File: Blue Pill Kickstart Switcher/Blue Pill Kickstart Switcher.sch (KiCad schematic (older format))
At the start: 23 parts, among them J1 Conn_01x02, J2 Conn_01x03, J3 Conn_01x03, J4 Conn_01x04, J5 Conn_01x03, J6 Conn_01x02, J7 Conn_01x02, J8 Conn_01x02, J9 Conn_01x02, U1 Conn_02x21_Counter_Clockwise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

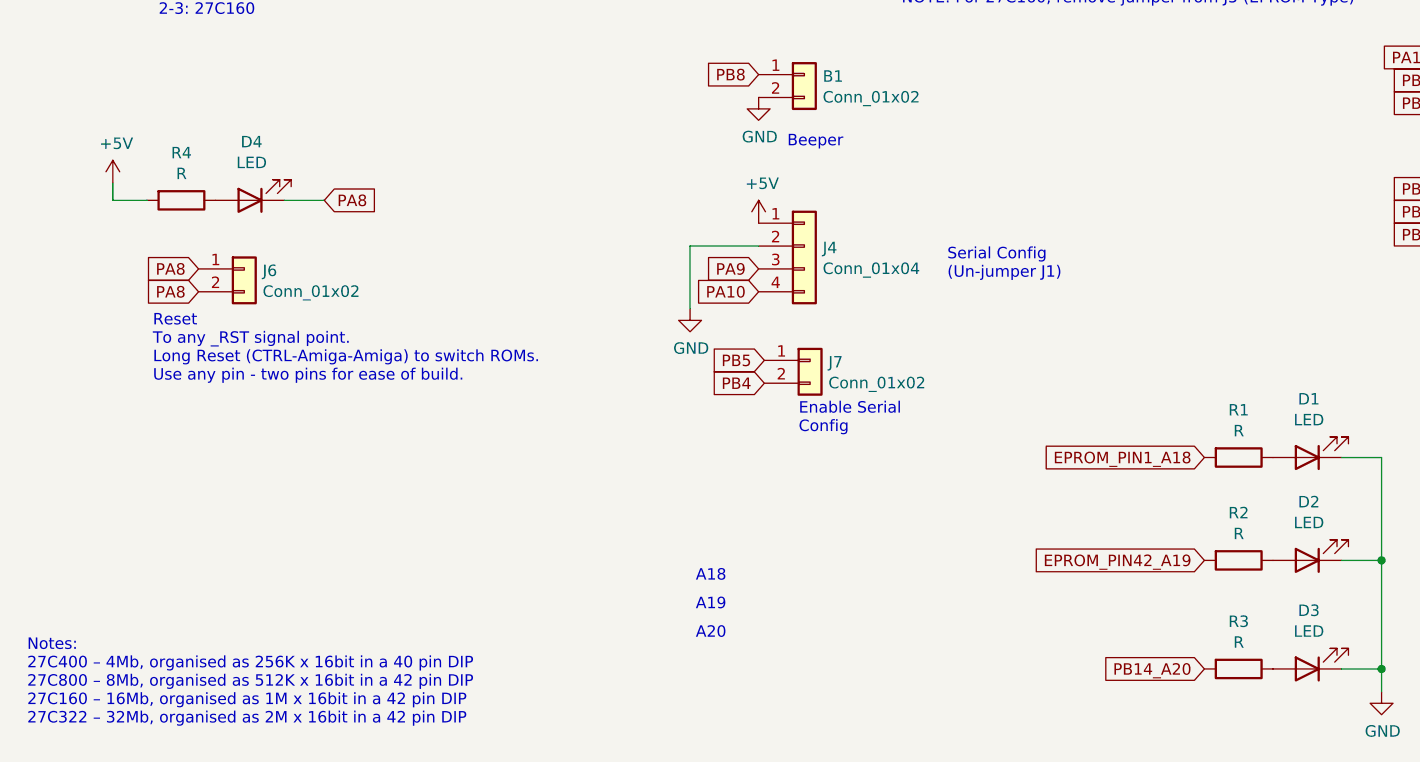
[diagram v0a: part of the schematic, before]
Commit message: Show resistor values in silk screen
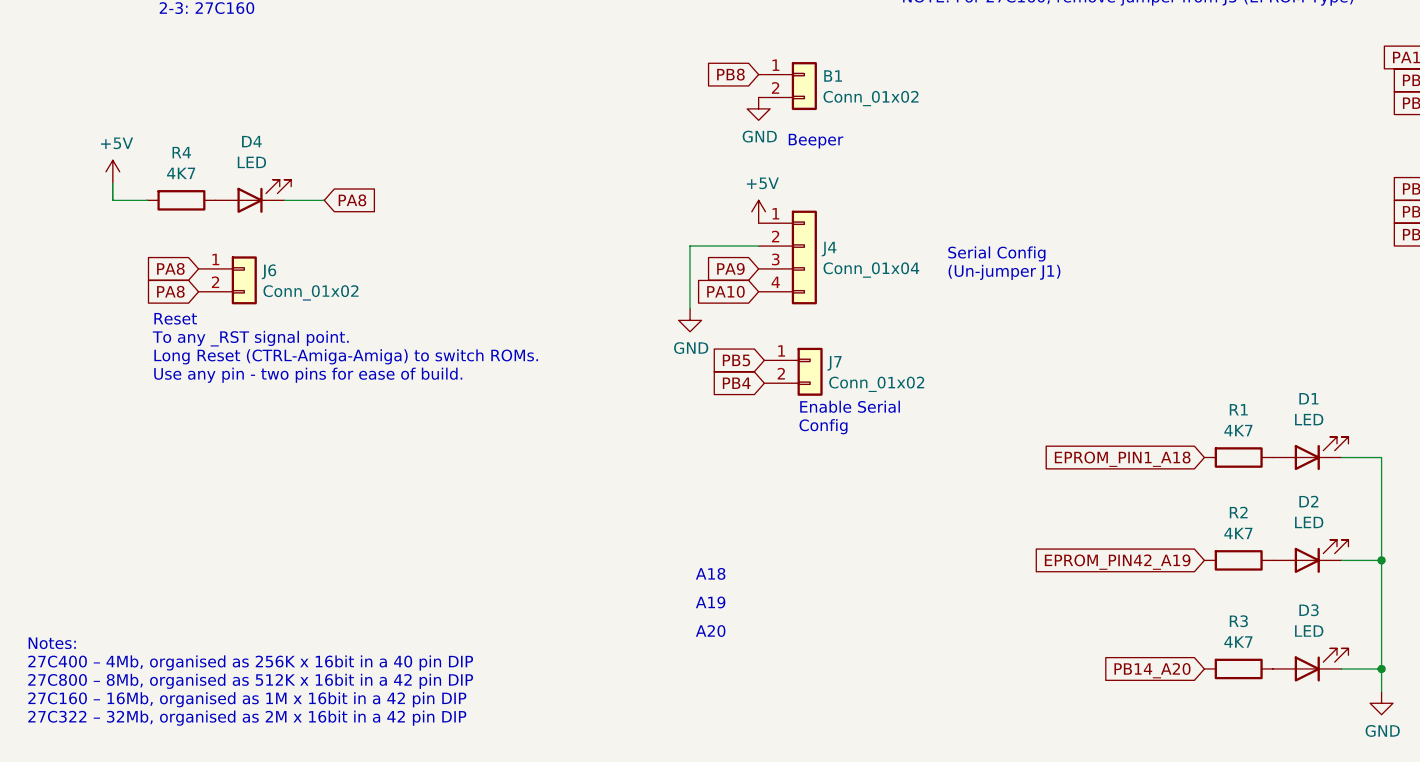
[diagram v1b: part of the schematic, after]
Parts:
- R1, R2, R3, R4: value R -> 4K7
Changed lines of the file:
@@
 P 5875 6500
 F 0 "R1" V 5668 6500 50  0000 C CNN
-F 1 "R" V 5759 6500 50  0000 C CNN
+F 1 "4K7" V 5759 6500 50  0000 C CNN
 F 2 "Resistor_SMD:R_0805_2012Metric_Pad1.20x1.40mm_HandSolder" V 5805 6500 50  0001 C CNN
 F 3 "~" H 5875 6500 50  0001 C CNN
@@
 P 5875 6950
 F 0 "R2" V 5668 6950 50  0000 C CNN
-F 1 "R" V 5759 6950 50  0000 C CNN
+F 1 "4K7" V 5759 6950 50  0000 C CNN
 F 2 "Resistor_SMD:R_0805_2012Metric_Pad1.20x1.40mm_HandSolder" V 5805 6950 50  0001 C CNN
 F 3 "~" H 5875 6950 50  0001 C CNN
@@
 P 5875 7425
 F 0 "R3" V 5668 7425 50  0000 C CNN
-F 1 "R" V 5759 7425 50  0000 C CNN
+F 1 "4K7" V 5759 7425 50  0000 C CNN
 F 2 "Resistor_SMD:R_0805_2012Metric_Pad1.20x1.40mm_HandSolder" V 5805 7425 50  0001 C CNN
 F 3 "~" H 5875 7425 50  0001 C CNN
@@
 P 1250 5375
 F 0 "R4" V 1043 5375 50  0000 C CNN
-F 1 "R" V 1134 5375 50  0000 C CNN
+F 1 "4K7" V 1134 5375 50  0000 C CNN
 F 2 "Resistor_SMD:R_0805_2012Metric_Pad1.20x1.40mm_HandSolder" V 1180 5375 50  0001 C CNN
 F 3 "~" H 1250 5375 50  0001 C CNN
